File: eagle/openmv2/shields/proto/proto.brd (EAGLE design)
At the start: 35.6 x 26.7 mm, 2 parts

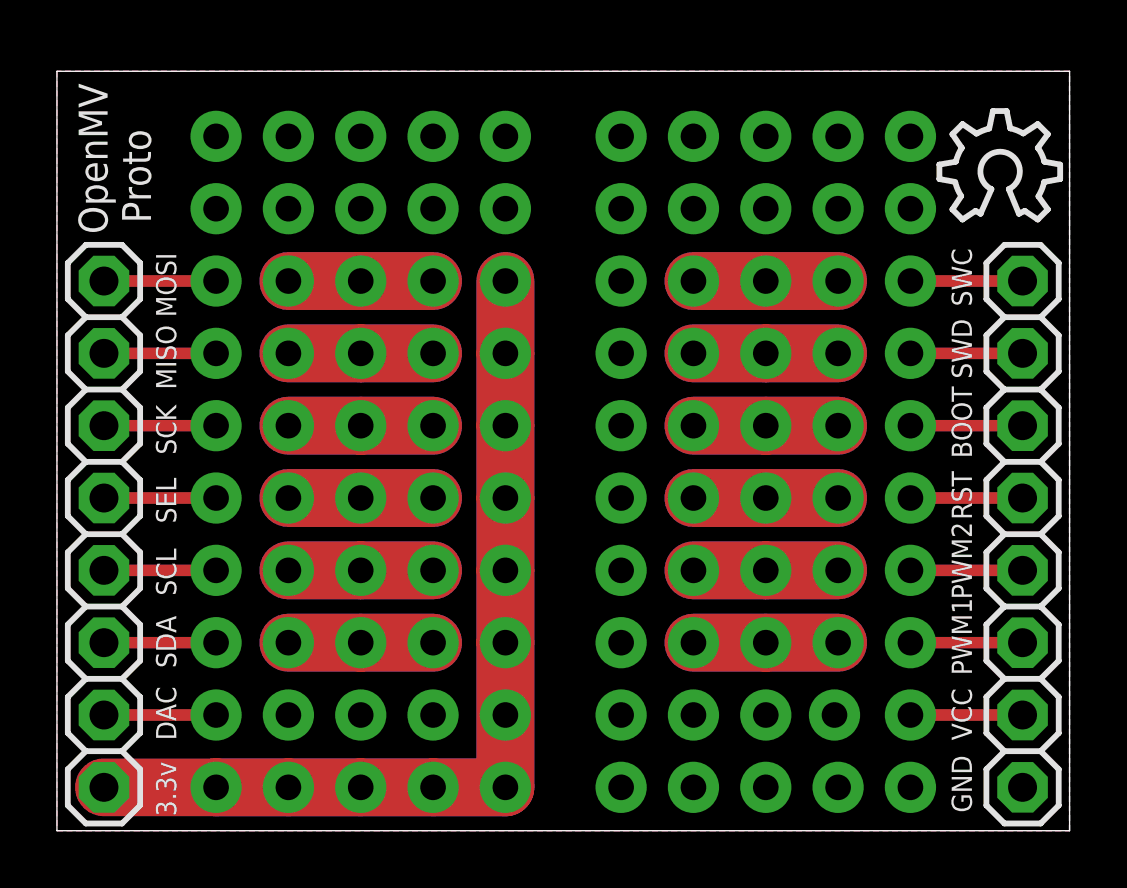
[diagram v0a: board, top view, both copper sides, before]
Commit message: Update shields silk-screen.
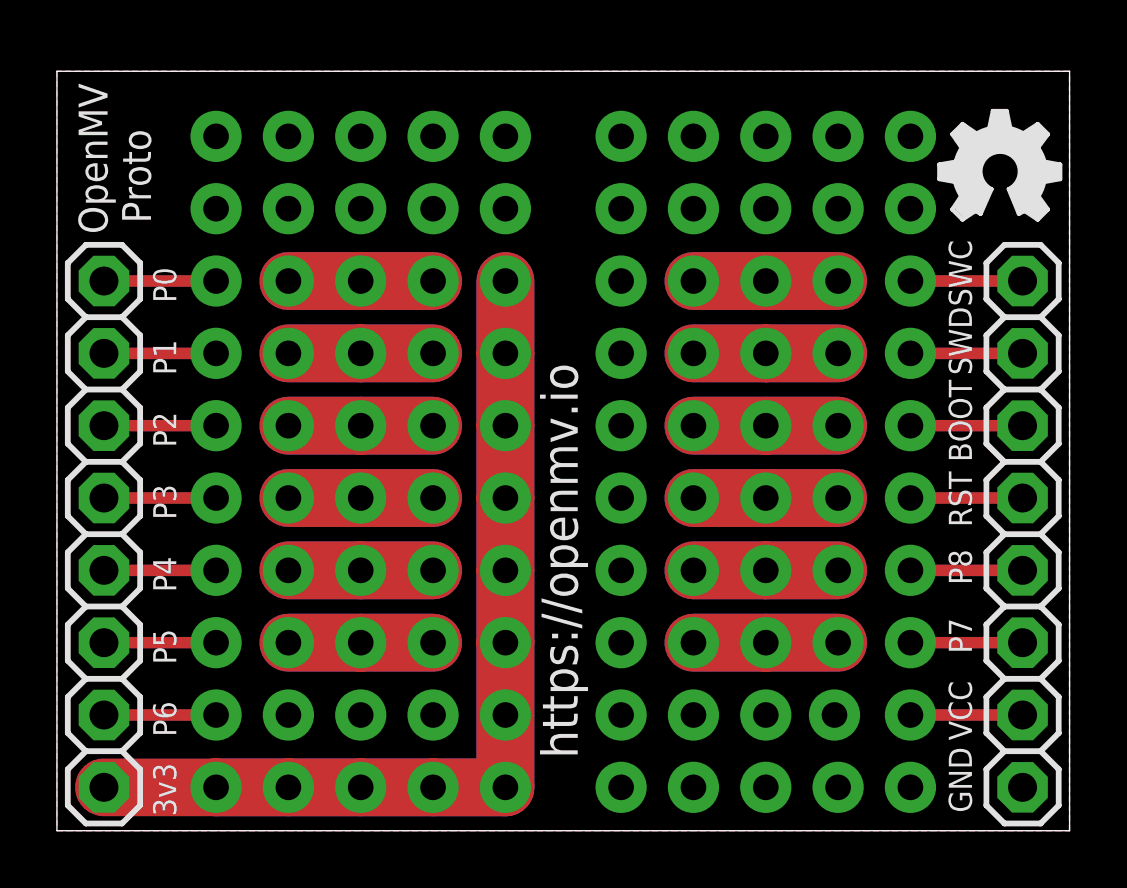
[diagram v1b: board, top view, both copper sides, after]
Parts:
- removed LOGO1: OSHW_LOGO_8MILX0150-NT, iofault:OSHW_8X150_NOTEXT
- added U$1: (no value), iofault:OSHW_FILLX150_NOTEXT
- added U$3: (no value), openmv:ROHS
- added U$4: (no value), openmv:WEEE
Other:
- board text added: "3v3"
- board text added: "P0"
- board text added: "P1"
- board text added: "P2"
- board text added: "P3"
- board text added: "P4"
- board text added: "P5"
- board text added: "P6"
- board text added: "P7"
- board text added: "P8"
- board text added: "https://openmv.io"
- board text removed: "0.5 oz copper"
- board text removed: "1 oz copper"
- board text removed: "3.3v"
- board text removed: "47 mil core"
- board text removed: "6.7 mil prepreg"
- board text removed: "Antenna trace 12mils (50Ohms impedance)"
- board text removed: "DAC"
- board text removed: "MISO"
- board text removed: "MOSI"
- board text removed: "PWM1"
- board text removed: "PWM2"
- board text removed: "SCK"
- board text removed: "SCL"
- board text removed: "SDA"
- board text removed: "SEL"
- board text removed: "Stackup:"
- board text removed: "er is 3.66"
